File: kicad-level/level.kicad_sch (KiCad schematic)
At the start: 6 parts, among them J1 Conn_01x01_Pin, J2 Conn_01x08_Pin, J3 Conn_01x01_Pin, U1 ULN2803A_C845537

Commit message: Revert "erreur pcb, com a la masse"
This reverts commit de789b6cb290ad22ceee4c73f03ad83cfbf3b982.
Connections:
- net GND: now also U1.10 (COM)
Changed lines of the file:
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@@
 	(paper "A4")
+	(junction
+		(at 167.64 127)
+		(diameter 0)
+		(color 0 0 0 0)
+	)
 	(junction
 		(at 154.94 127)
@@
 		)
 		(stroke
+			(width 0)
+			(type default)
+		)
+	)
+	(wire
+		(pts
+			(xy 167.64 90.17) (xy 167.64 127)
+		)
+		(stroke

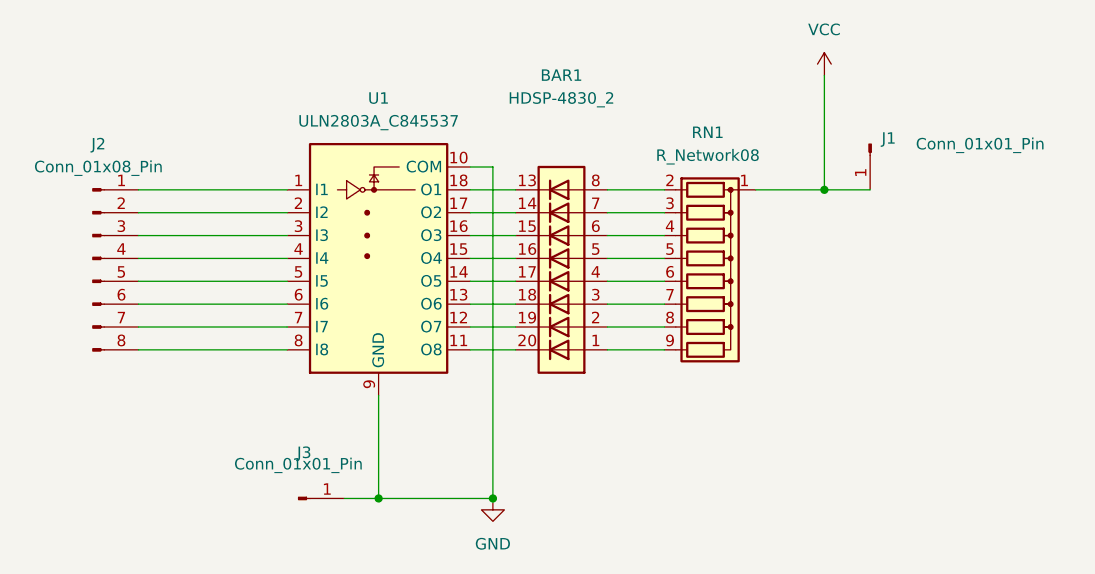
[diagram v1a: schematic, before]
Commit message: erreur pcb, com a la masse
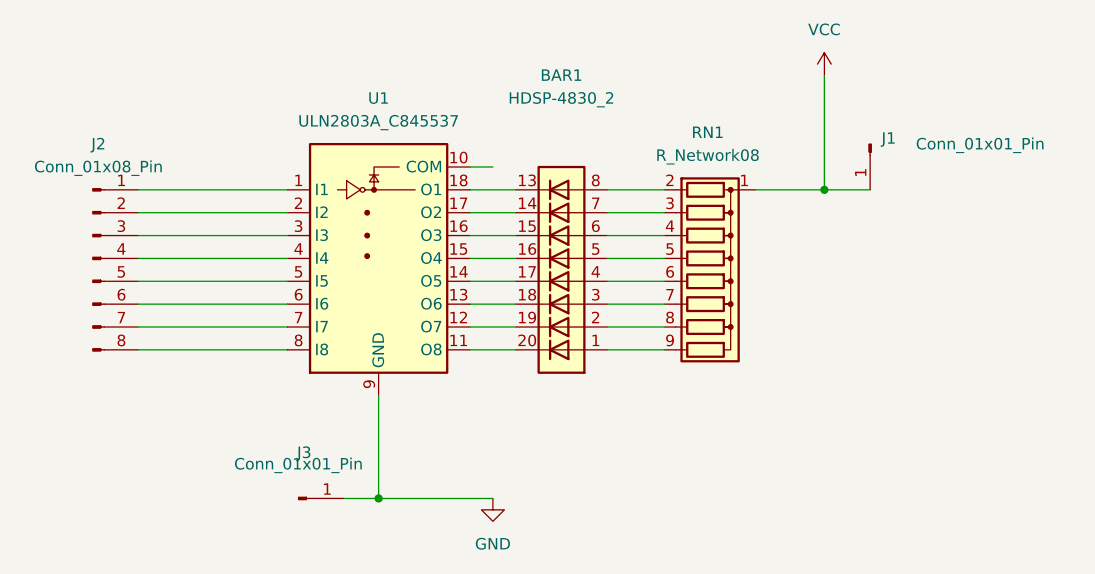
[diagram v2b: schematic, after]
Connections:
- net GND: no longer U1.10 (COM)
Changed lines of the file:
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@@
 	(paper "A4")
-	(junction
-		(at 167.64 127)
-		(diameter 0)
-		(color 0 0 0 0)
-	)
 	(junction
 		(at 154.94 127)
@@
 		)
 		(stroke
-			(width 0)
-			(type default)
-		)
-	)
-	(wire
-		(pts
-			(xy 167.64 90.17) (xy 167.64 127)
-		)
-		(stroke
